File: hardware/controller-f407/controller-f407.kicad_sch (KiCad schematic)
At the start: 0 parts

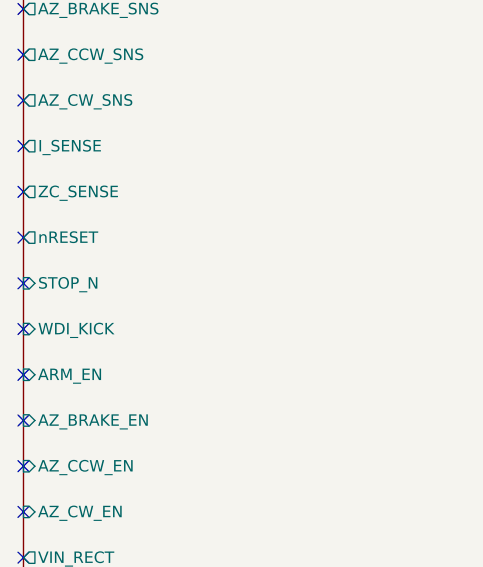
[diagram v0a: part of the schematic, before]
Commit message: Drop the Drive supervisor and the STOP pin.
The TPS3823, Q8, Q9, and their passives leave the rotor sheet. ARM_EN drives the relay FET, with the pulldowns holding a high-Z gate off. STOP stays a Station command. ADR 0021 is Accepted, including the below-POR check and the case that still fails.

Co-authored-by: Jeffrey Millar <wa1hco@users.noreply.github.com>
Co-authored-by: Cursor Agent <cursoragent@cursor.com>
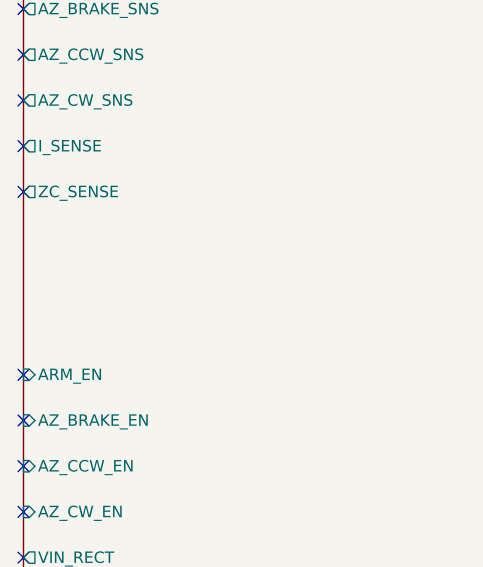
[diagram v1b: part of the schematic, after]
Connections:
- no-connect marks 19 -> 16
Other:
- sheet rotor_drive ports: added none; removed STOP_N, WDI_KICK, nRESET
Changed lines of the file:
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@@
-	)
-	(no_connect
-		(at 86.36 101.6)
 	)
 	(no_connect
@@
 	(no_connect
 		(at 86.36 137.16)
-	)
-	(no_connect
-		(at 86.36 106.68)
-	)
-	(no_connect
-		(at 86.36 111.76)
 	)
 	(no_connect
@@
 			(effects
 				(font
-					(size 1.27 1.27)
-				)
-				(justify right)
-			)
-		)
-		(pin "WDI_KICK" input
-			(at 86.36 111.76 180)
-			(effects
-				(font
-					(size 1.27 1.27)
-				)
-				(justify right)
-			)
-		)
-		(pin "STOP_N" input
-			(at 86.36 106.68 180)
-			(effects
-				(font
-					(size 1.27 1.27)
-				)
-				(justify right)
-			)
-		)
-		(pin "nRESET" output
-			(at 86.36 101.6 180)
-			(effects
-				(font

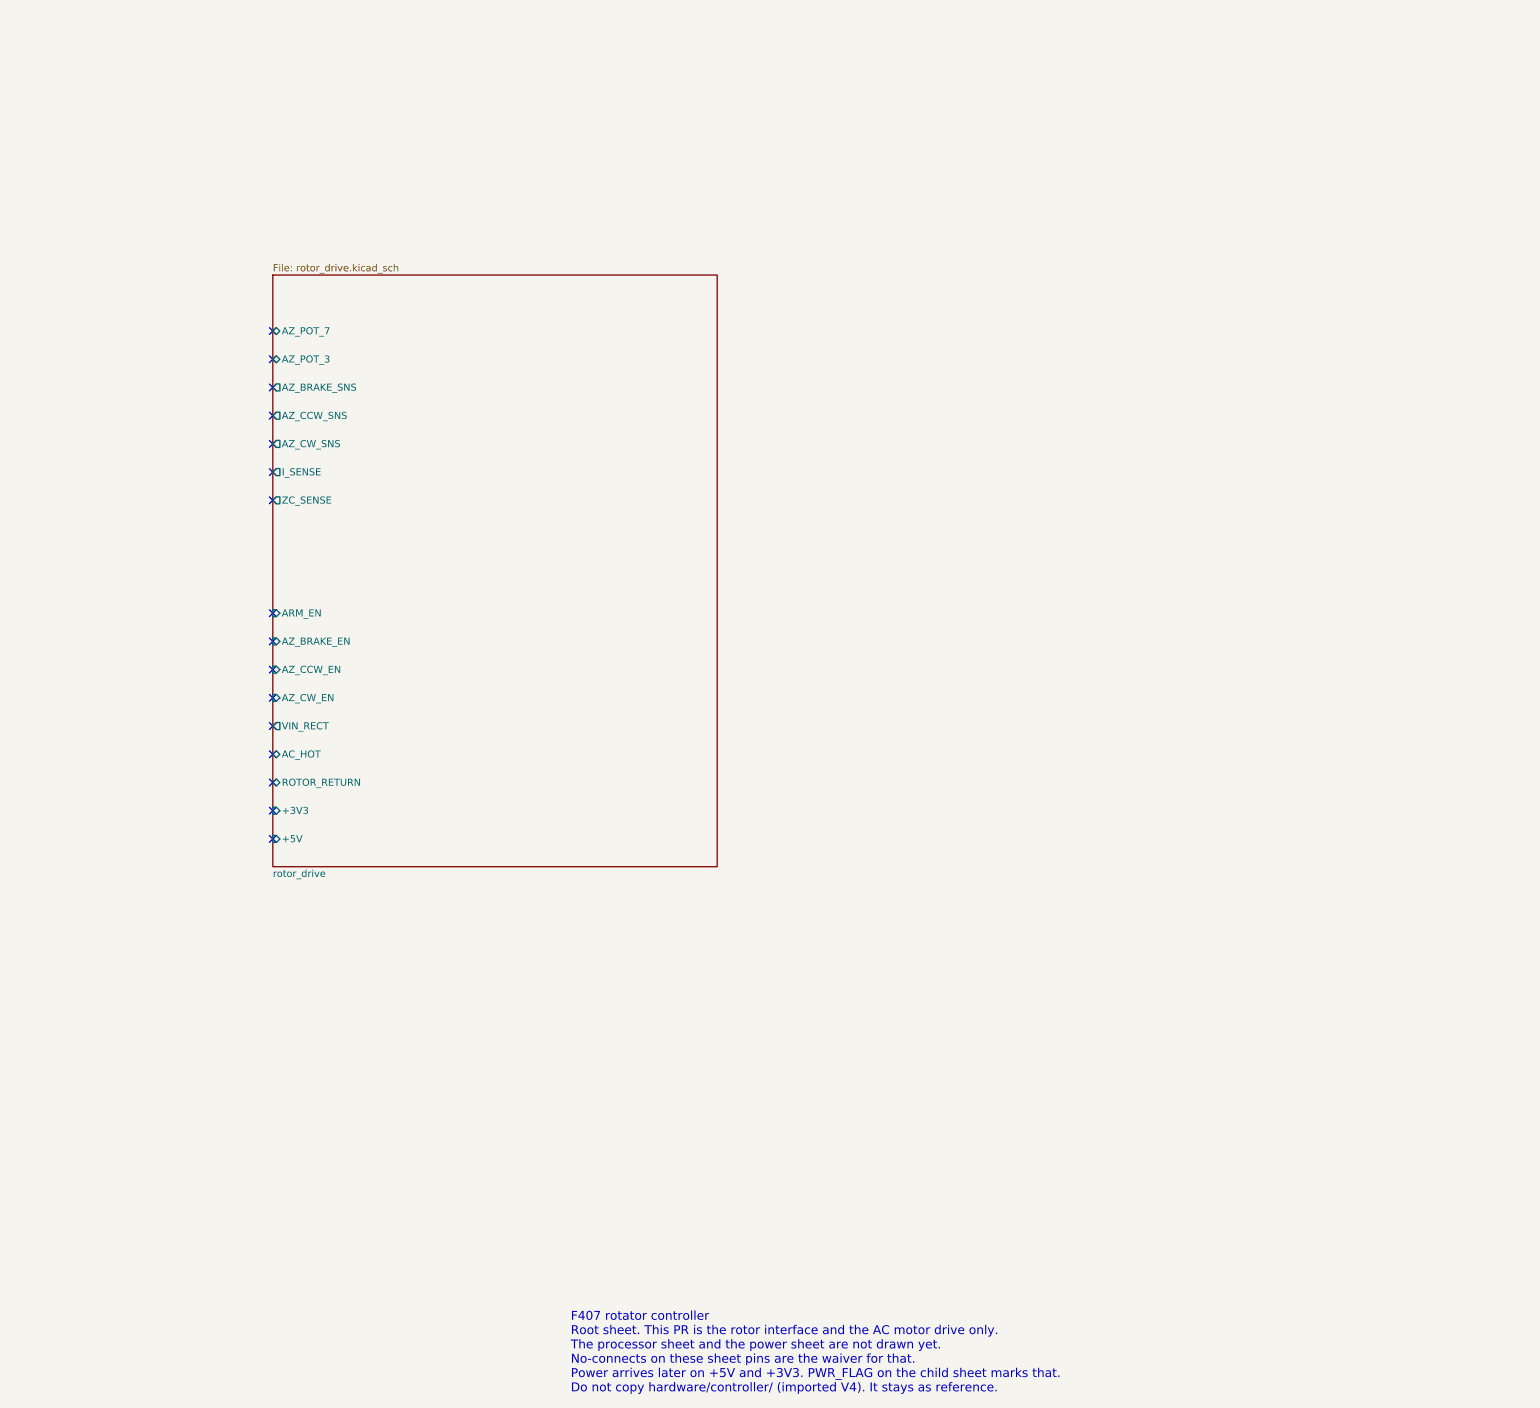
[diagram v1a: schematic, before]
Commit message: Add the Drive MCU and analog sheets, and tidy the triac page (#12)
* Add the Drive MCU and analog sheets, and tidy the triac page.

Tie the dangling ROTOR_RETURN label to GNDPWR, clear overlapping field
text without moving owner-placed parts, and hang drive_mcu and
analog_input off the root. Pin assignment follows ADR 0021.

Co-authored-by: Jeffrey Millar <wa1hco@users.noreply.github.com>
Co-authored-by: Cursor Agent <cursoragent@cursor.com>

* Rename the relay net back to ARM_EN and drop the dangling stub.

The owner's label text is ARM_EN again, in place. One pulldown remains
on each gate line. TR1 conditioning stays on the rotor sheet.

Co-authored-by: Jeffrey Millar <wa1hco@users.noreply.github.com>
Co-authored-by: Cursor Agent <cursoragent@cursor.com>

* Record the 57d43f9 rotor sheet in owner_frozen.json.

The layout tweak did not add or remove text keys. The ARM_EN label and the removed stub keep the same keys. Positions are not stored and nothing is moved.

Co-authored-by: Jeffrey Millar <wa1hco@users.noreply.github.com>

---------

Co-authored-by: Cursor Agent <cursoragent@cursor.com>
Co-authored-by: Jeffrey Millar <wa1hco@users.noreply.github.com>
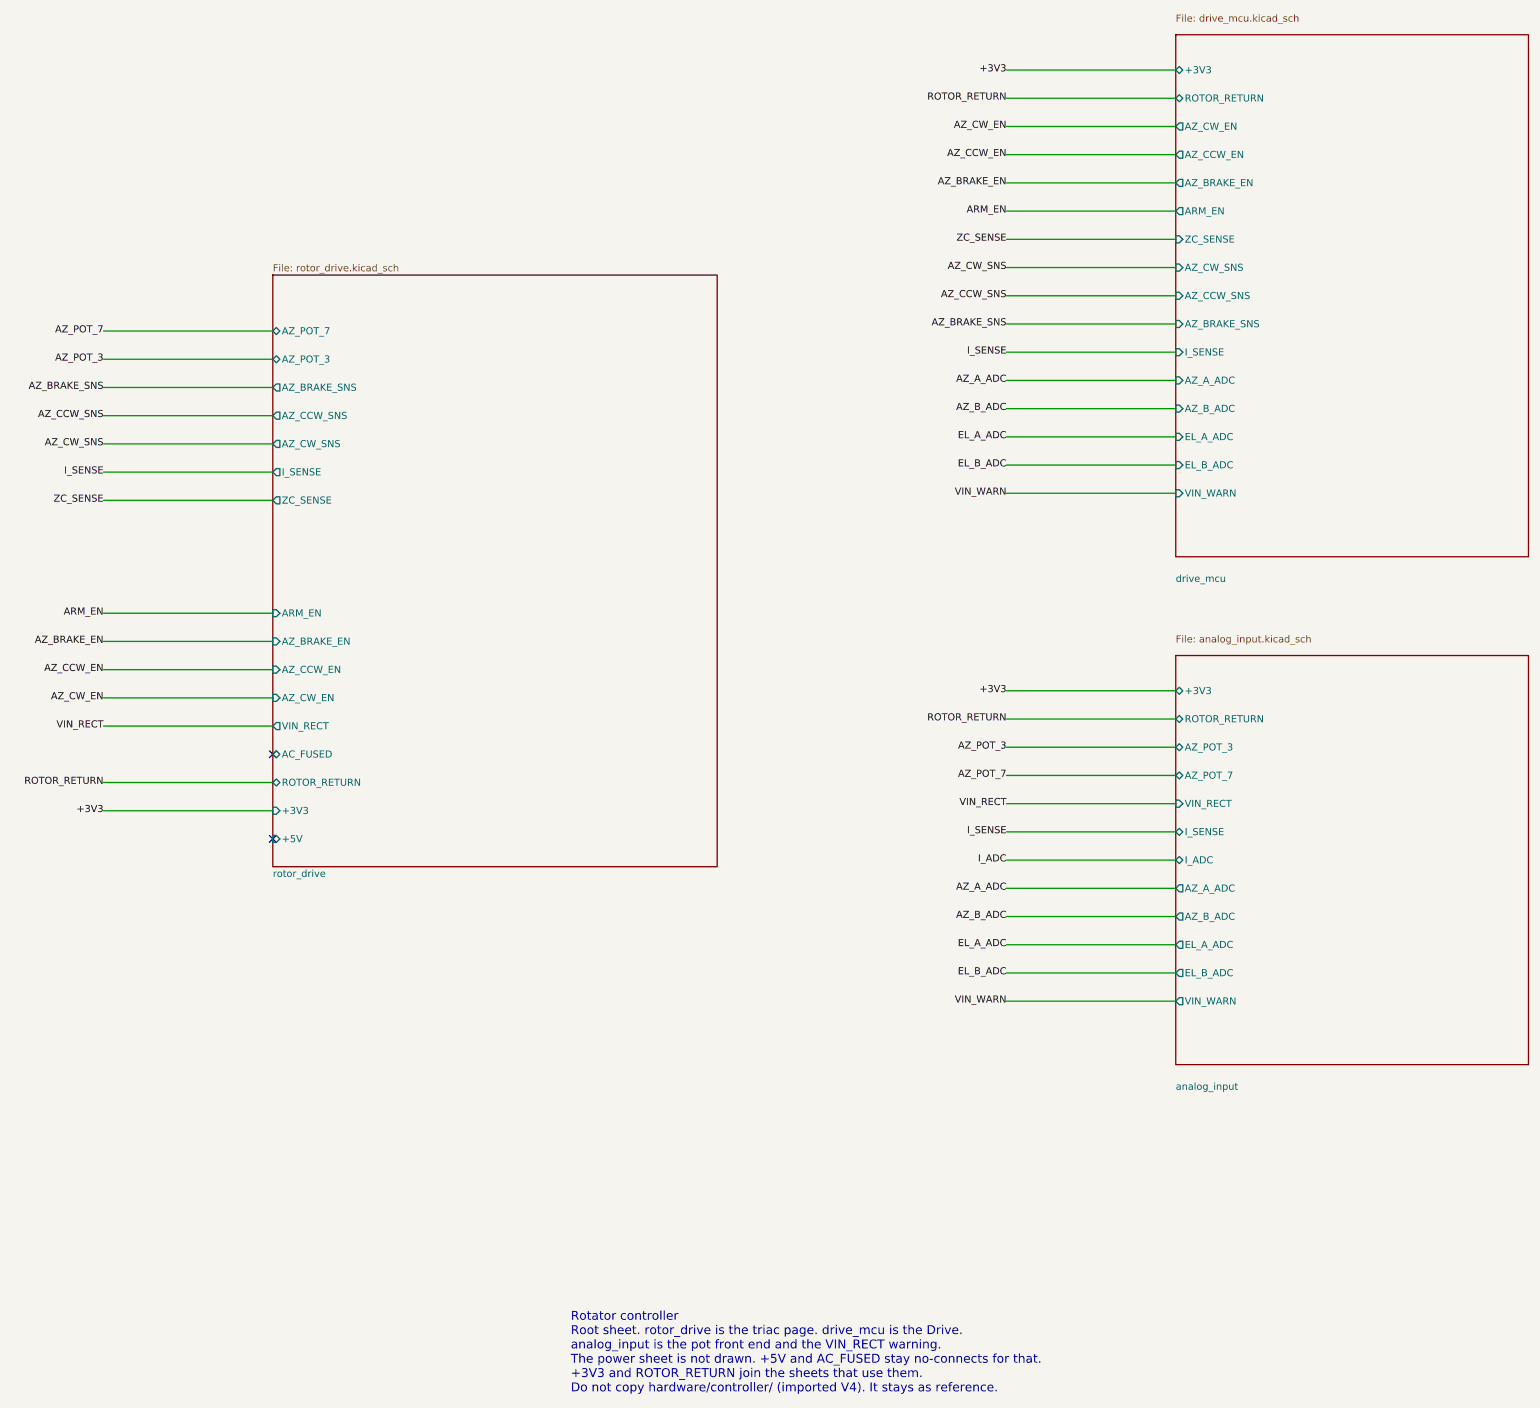
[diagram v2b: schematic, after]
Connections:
- no-connect marks 16 -> 2
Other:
- added sheet analog_input (analog_input.kicad_sch)
- added sheet drive_mcu (drive_mcu.kicad_sch)
- sheet rotor_drive ports: added AC_FUSED; removed AC_HOT
- note added: "Rotator controller Root sheet. rotor_drive is the triac page. drive_mcu is the Drive. analog_input is the pot front end and the VIN_RECT warning. The power sheet is not drawn. +5V and AC_FUSED stay no-connects for that. +3V3 and ROTOR_RETURN join the sheets that use them. Do not copy hardware/controller/ (imported V4). It stays as reference."
- note removed: "F407 rotator controller Root sheet. This PR is the rotor interface and the AC motor drive only. The processor sheet and the power sheet are not drawn yet. No-connects on these sheet pins are the waiver for that. Power arrives later on +5V and +3V3. PWR_FLAG on the child sheet marks that. Do not copy hardware/controller/ (imported V4). It stays as reference."
